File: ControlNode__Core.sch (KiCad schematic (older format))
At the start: 1 part

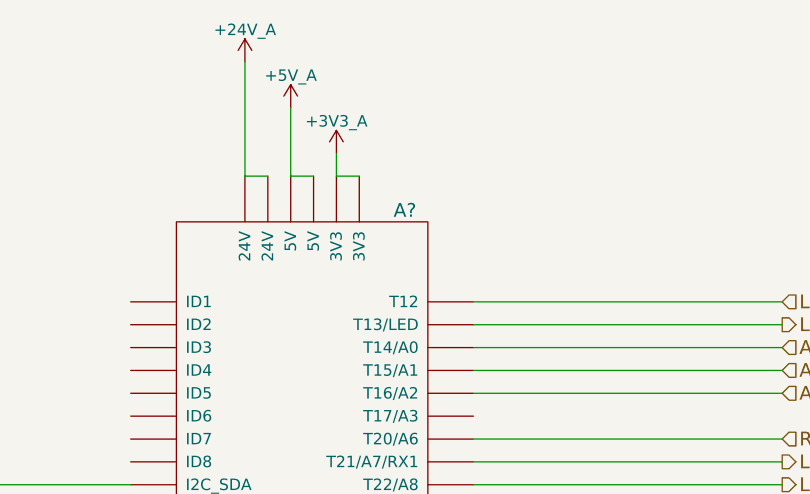
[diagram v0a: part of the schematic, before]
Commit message: Update 10K pullups, 100R on RS422's and additional bypass caps.
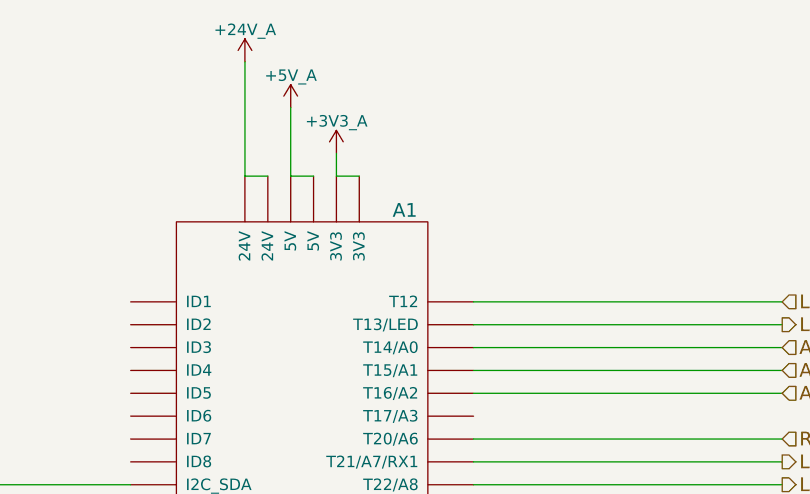
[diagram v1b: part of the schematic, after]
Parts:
- gave numbers to parts that had none: 1
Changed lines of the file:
@@
 $EndDescr
 $Comp
-L NODE_CORE_CONNECTOR A?
+L NODE_CORE_CONNECTOR A1
 U 1 1 575CAC23
 P 8300 4200
-F 0 "A?" H 8750 5600 60  0000 C CNN
+F 0 "A1" H 8750 5600 60  0000 C CNN
 F 1 "NODE_CORE_CONNECTOR" H 9000 2650 60  0000 C CNN
 F 2 "" H 8300 4200 60  0000 C CNN
@@
 $EndComp
 $Comp
-L +24V_A #PWR?
+L +24V_A #PWR75
 U 1 1 575CAC5C
 P 8050 2150
-F 0 "#PWR?" H 8050 2000 50  0001 C CNN
+F 0 "#PWR75" H 8050 2000 50  0001 C CNN
 F 1 "+24V_A" H 8050 2290 50  0000 C CNN
 F 2 "" H 8050 2150 60  0000 C CNN
@@
 $EndComp
 $Comp
-L +5V_A #PWR?
+L +5V_A #PWR77
 U 1 1 575CAC72
 P 8250 2350
-F 0 "#PWR?" H 8250 2200 50  0001 C CNN
+F 0 "#PWR77" H 8250 2200 50  0001 C CNN
 F 1 "+5V_A" H 8250 2490 50  0000 C CNN
 F 2 "" H 8250 2350 60  0000 C CNN
@@
 $EndComp
 $Comp
-L +3V3_A #PWR?
+L +3V3_A #PWR78
 U 1 1 575CAC88
 P 8450 2550
-F 0 "#PWR?" H 8450 2400 50  0001 C CNN
+F 0 "#PWR78" H 8450 2400 50  0001 C CNN
 F 1 "+3V3_A" H 8450 2690 50  0000 C CNN
 F 2 "" H 8450 2550 60  0000 C CNN
@@
 	8450 2650 8550 2650
 $Comp
-L GNDD #PWR?
+L GNDD #PWR76
 U 1 1 575CACE0
 P 8200 5900
-F 0 "#PWR?" H 8200 5650 50  0001 C CNN
+F 0 "#PWR76" H 8200 5650 50  0001 C CNN
 F 1 "GNDD" H 8200 5750 50  0000 C CNN
 F 2 "" H 8200 5900 50  0000 C CNN
